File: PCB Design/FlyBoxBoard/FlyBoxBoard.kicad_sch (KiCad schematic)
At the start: 42 parts, among them J1 5V in, J10 RED, J11 GREEN, J12 WHITE, J13 INFRARED, J14 LCD Screen, J15 SD card reader, J16 5K Ohms, J17 5K Ohms, J18 ESP 32 Left Side extra pinouts, J19 ESP 32 Left Side extra pinouts, J2 12V in, J20 Transistor, J21 Logic Level LV pins, J22 Potentiometer, J23 Logic Level Left Side LV, J25 ESP 32 Right Side extra pinou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, J26 BuckPuck IR, J27 Logic Level Right Side HV, J28 Logic Level HV pins, J29 5K Ohms, J3 ESP 32 Left Side, J30 5K Ohms, J31 5K Ohms, J32 5K Ohms, J33 5K Ohms, J34 5K Ohms, J35 Transistor, J36 Transistor, J37 Transistor, J38 BuckPuck White, J39 BuckPuck Green, J4 Real Time Controller, J40 BuckPuck Red, J5 ESP 32 Right Side, J6 Rotary Knob, J9 FANS

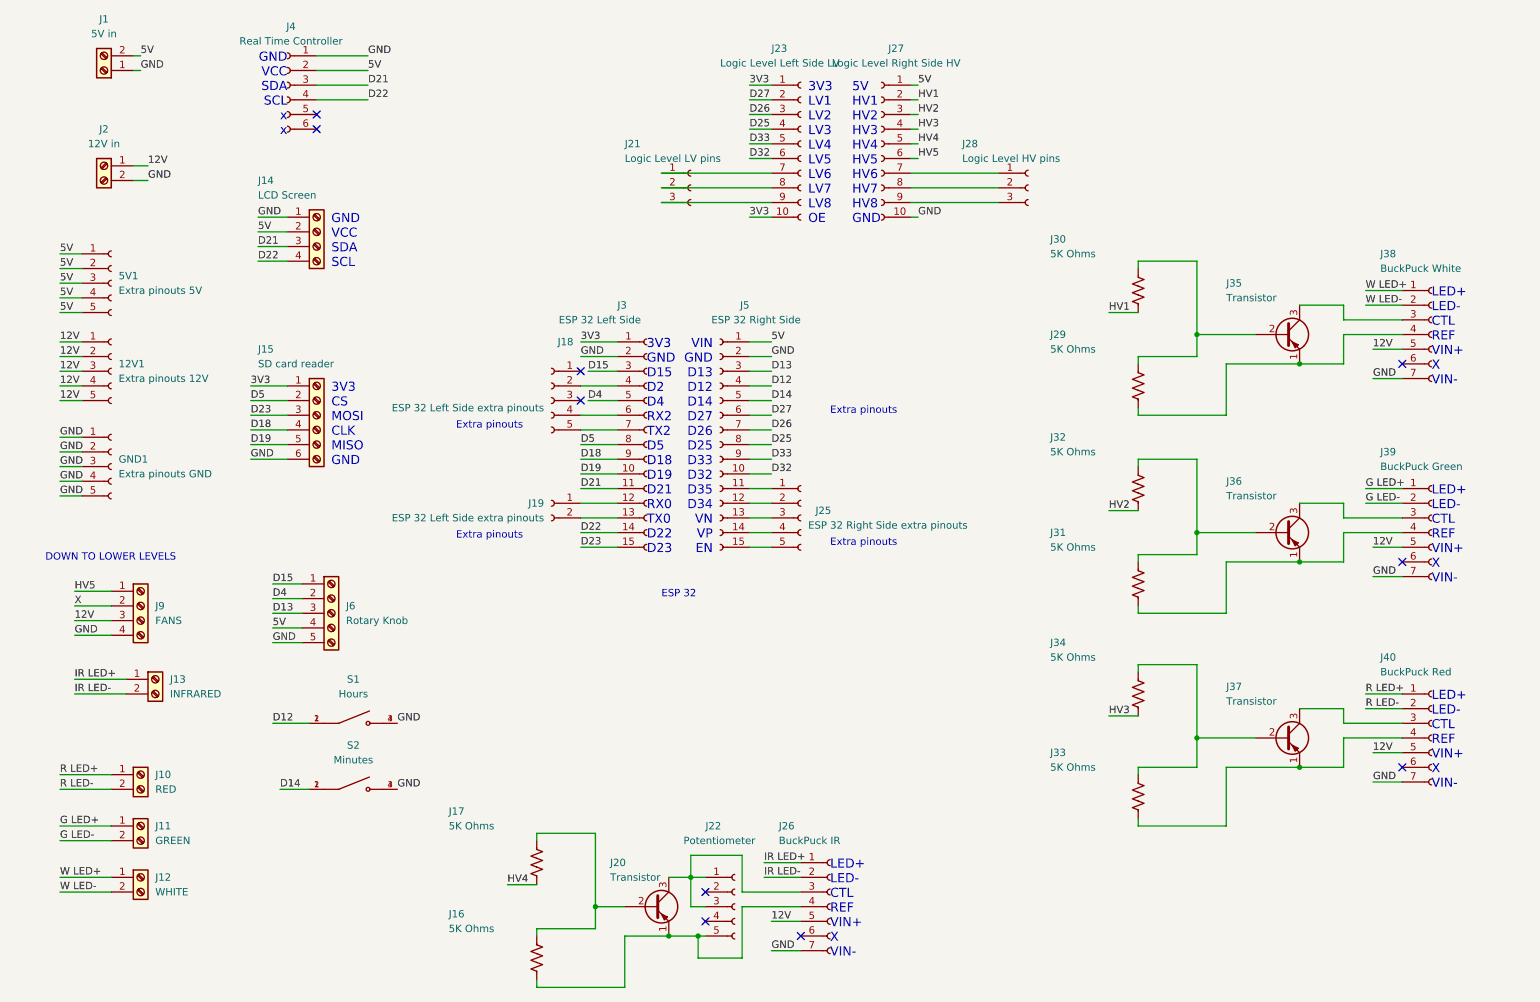
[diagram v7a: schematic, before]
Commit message: Shrunk vias, fixed ohms and XV1 labels
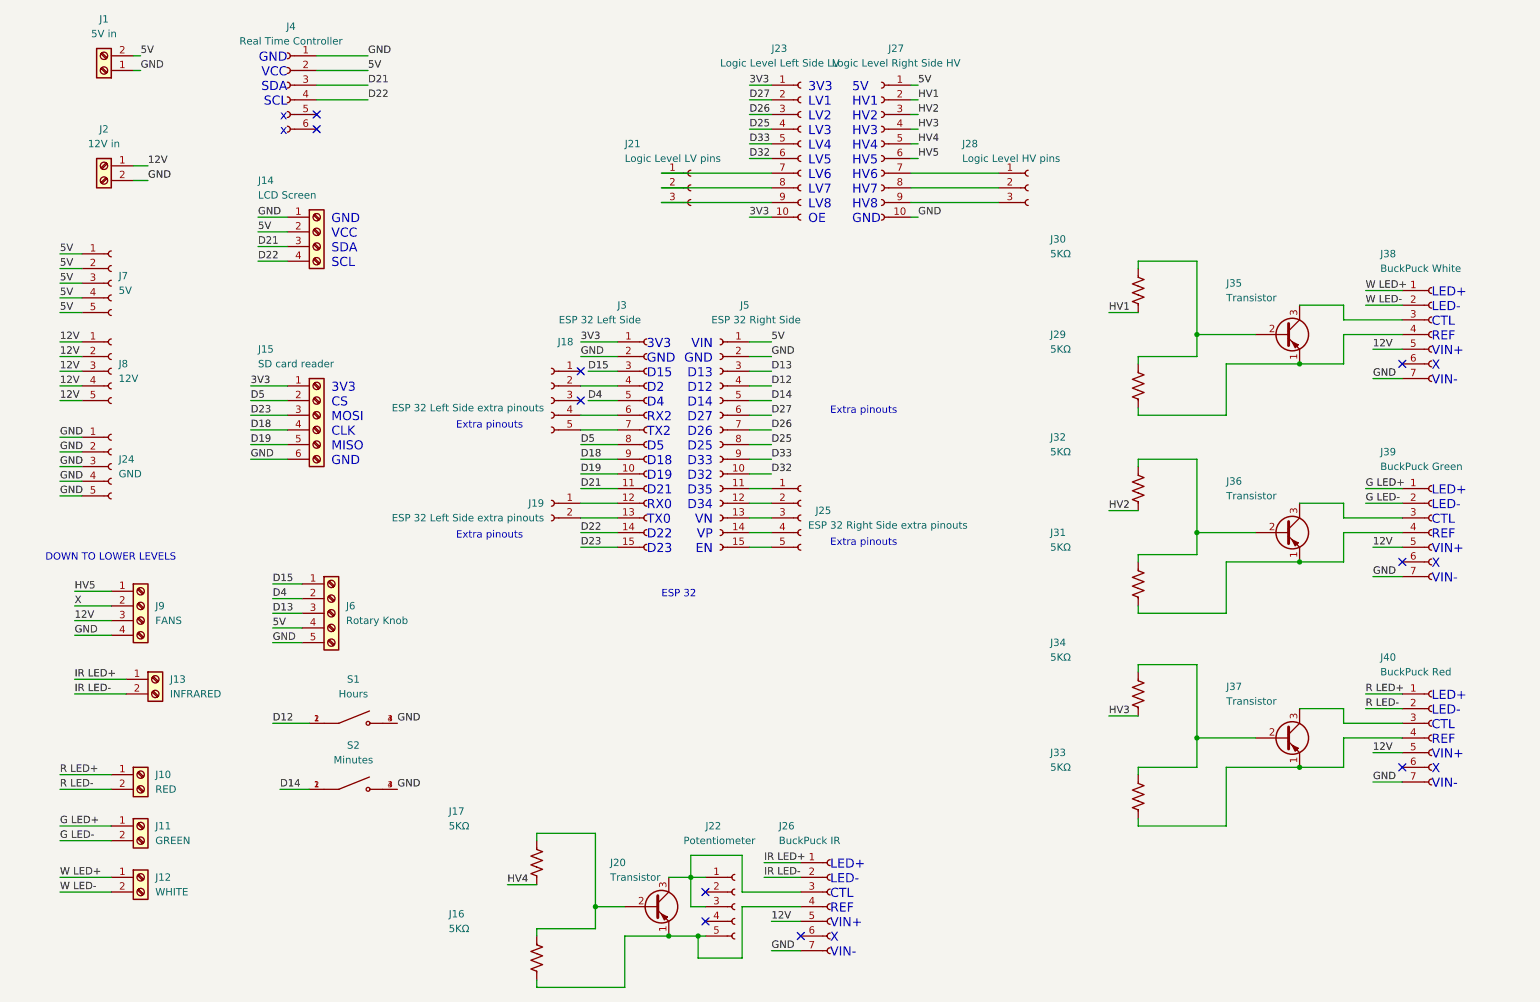
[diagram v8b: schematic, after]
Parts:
- J16, J17, J29, J30, J31, J32, J33, J34: value 5K Ohms -> 5KΩ
- J24: renamed from GND1; value Extra pinouts GND -> GND
- J7: renamed from 5V1; value Extra pinouts 5V -> 5V
- J8: renamed from 12V1; value Extra pinouts 12V -> 12V
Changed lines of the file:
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@@
   (symbol (lib_id "Connector:Conn_01x05_Female") (at 26.67 64.77 0) (unit 1)
     (in_bom yes) (on_board yes) (fields_autoplaced)
-    (property "Reference" "5V1" (id 0) (at 27.94 63.4999 0)
-      (effects (font (size 1.27 1.27)) (justify left))
-    )
-    (property "Value" "Extra pinouts 5V" (id 1) (at 27.94 66.0399 0)
+    (property "Reference" "J7" (id 0) (at 27.94 63.4999 0)
+      (effects (font (size 1.27 1.27)) (justify left))
+    )
+    (property "Value" "5V" (id 1) (at 27.94 66.0399 0)
       (effects (font (size 1.27 1.27)) (justify left))
     )
@@
       (effects (font (size 1.27 1.27)) (justify left))
     )
-    (property "Value" "5K Ohms" (id 1) (at 189.23 110.49 0)
+    (property "Value" "5KΩ" (id 1) (at 189.23 110.49 0)
       (effects (font (size 1.27 1.27)) (justify left))
     )
@@
       (effects (font (size 1.27 1.27)) (justify left))
     )
-    (property "Value" "5K Ohms" (id 1) (at 189.23 76.2 0)
+    (property "Value" "5KΩ" (id 1) (at 189.23 76.2 0)
       (effects (font (size 1.27 1.27)) (justify left))
     )
@@
   (symbol (lib_id "Connector:Conn_01x05_Female") (at 26.67 80.01 0) (unit 1)
     (in_bom yes) (on_board yes) (fields_autoplaced)
-    (property "Reference" "12V1" (id 0) (at 27.94 78.7399 0)
-      (effects (font (size 1.27 1.27)) (justify left))
-    )
-    (property "Value" "Extra pinouts 12V" (id 1) (at 27.94 81.2799 0)
+    (property "Reference" "J8" (id 0) (at 27.94 78.7399 0)
+      (effects (font (size 1.27 1.27)) (justify left))
+    )
+    (property "Value" "12V" (id 1) (at 27.94 81.2799 0)
       (effects (font (size 1.27 1.27)) (justify left))
     )
@@
   (symbol (lib_id "Connector:Conn_01x05_Female") (at 26.67 96.52 0) (unit 1)
     (in_bom yes) (on_board yes) (fields_autoplaced)
-    (property "Reference" "GND1" (id 0) (at 27.94 95.2499 0)
-      (effects (font (size 1.27 1.27)) (justify left))
-    )
-    (property "Value" "Extra pinouts GND" (id 1) (at 27.94 97.7899 0)
+    (property "Reference" "J24" (id 0) (at 27.94 95.2499 0)
+      (effects (font (size 1.27 1.27)) (justify left))
+    )
+    (property "Value" "GND" (id 1) (at 27.94 97.7899 0)
       (effects (font (size 1.27 1.27)) (justify left))
     )
@@
       (effects (font (size 1.27 1.27)) (justify left))
     )
-    (property "Value" "5K Ohms" (id 1) (at 189.23 148.59 0)
+    (property "Value" "5KΩ" (id 1) (at 189.23 148.59 0)
       (effects (font (size 1.27 1.27)) (justify left))
     )
@@
       (effects (font (size 1.27 1.27)) (justify left))
     )
-    (property "Value" "5K Ohms" (id 1) (at 189.23 59.69 0)
+    (property "Value" "5KΩ" (id 1) (at 189.23 59.69 0)
       (effects (font (size 1.27 1.27)) (justify left))
     )
@@
       (effects (font (size 1.27 1.27)) (justify left))
     )
-    (property "Value" "5K Ohms" (id 1) (at 85.09 176.53 0)
+    (property "Value" "5KΩ" (id 1) (at 85.09 176.53 0)
       (effects (font (size 1.27 1.27)) (justify left))
     )
@@
       (effects (font (size 1.27 1.27)) (justify left))
     )
-    (property "Value" "5K Ohms" (id 1) (at 189.23 129.54 0)
+    (property "Value" "5KΩ" (id 1) (at 189.23 129.54 0)
       (effects (font (size 1.27 1.27)) (justify left))
     )
@@
       (effects (font (size 1.27 1.27)) (justify left))
     )
-    (property "Value" "5K Ohms" (id 1) (at 189.23 93.98 0)
+    (property "Value" "5KΩ" (id 1) (at 189.23 93.98 0)
       (effects (font (size 1.27 1.27)) (justify left))
     )
@@
       (effects (font (size 1.27 1.27)) (justify left))
     )
-    (property "Value" "5K Ohms" (id 1) (at 85.09 158.75 0)
+    (property "Value" "5KΩ" (id 1) (at 85.09 158.75 0)
       (effects (font (size 1.27 1.27)) (justify left))
     )
@@
   )
   (symbol_instances
-    (path "/2481291e-206f-4136-b767-c88851d692f7"
-      (reference "5V1") (unit 1) (value "Extra pinouts 5V") (footprint "Connector_PinSocket_2.54mm:PinSocket_1x05_P2.54mm_Vertical")
-    )
-    (path "/6183f4c2-b8b4-40db-bb6c-bf761daf770e"
-      (reference "12V1") (unit 1) (value "Extra pinouts 12V") (footprint "Connector_PinSocket_2.54mm:PinSocket_1x05_P2.54mm_Vertical")
-    )
-    (path "/89950f7f-7114-4cb1-ae2e-fc47480a7284"
-      (reference "GND1") (unit 1) (value "Extra pinouts GND") (footprint "Connector_PinSocket_2.54mm:PinSocket_1x05_P2.54mm_Vertical")
-    )
     (path "/44c71451-ea99-4268-833f-b68e3d908475"
       (reference "J1") (unit 1) (value "5V in") (footprint "TerminalBlock:TerminalBlock_bornier-2_P5.08mm")
@@
       (reference "J6") (unit 1) (value "Rotary Knob") (footprint "TerminalBlock:TerminalBlock_bornier-5_P5.08mm")
     )
+    (path "/2481291e-206f-4136-b767-c88851d692f7"
+      (reference "J7") (unit 1) (value "5V") (footprint "Connector_PinSocket_2.54mm:PinSocket_1x05_P2.54mm_Vertical")
+    )
+    (path "/6183f4c2-b8b4-40db-bb6c-bf761daf770e"
+      (reference "J8") (unit 1) (value "12V") (footprint "Connector_PinSocket_2.54mm:PinSocket_1x05_P2.54mm_Vertical")
+    )
     (path "/bbae7729-1b1d-4e0d-b021-77b9c2200ef4"
       (reference "J9") (unit 1) (value "FANS") (footprint "TerminalBlock:TerminalBlock_bornier-4_P5.08mm")
@@
     )
     (path "/c0473f3f-82e6-418a-b889-dfcb5651b6e1"
-      (reference "J16") (unit 1) (value "5K Ohms") (footprint "Resistor_SMD:R_0805_2012Metric_Pad1.20x1.40mm_HandSolder")
+      (reference "J16") (unit 1) (value "5KΩ") (footprint "Resistor_SMD:R_0805_2012Metric_Pad1.20x1.40mm_HandSolder")
     )
     (path "/d2ffe9e0-42cd-49d3-9622-5c200a1d4d6b"
-      (reference "J17") (unit 1) (value "5K Ohms") (footprint "Resistor_SMD:R_0805_2012Metric_Pad1.20x1.40mm_HandSolder")
+      (reference "J17") (unit 1) (value "5KΩ") (footprint "Resistor_SMD:R_0805_2012Metric_Pad1.20x1.40mm_HandSolder")
     )
     (path "/857e8bbb-d58b-44f9-ba40-ff0fb25a9518"
@@
       (reference "J23") (unit 1) (value "Logic Level Left Side LV") (footprint "Connector_PinSocket_2.54mm:PinSocket_1x10_P2.54mm_Vertical")
     )
+    (path "/89950f7f-7114-4cb1-ae2e-fc47480a7284"
+      (reference "J24") (unit 1) (value "GND") (footprint "Connector_PinSocket_2.54mm:PinSocket_1x05_P2.54mm_Vertical")
+    )
     (path "/108235f0-b9d5-497f-8a9f-f494ab16621f"
       (reference "J25") (unit 1) (value "ESP 32 Right Side extra pinouts") (footprint "Connector_PinSocket_2.54mm:PinSocket_1x05_P2.54mm_Vertical")
@@
     )
     (path "/60499b43-5f6c-4a6f-a2eb-3aa9716cc0ba"
-      (reference "J29") (unit 1) (value "5K Ohms") (footprint "Resistor_SMD:R_0805_2012Metric_Pad1.20x1.40mm_HandSolder")
+      (reference "J29") (unit 1) (value "5KΩ") (footprint "Resistor_SMD:R_0805_2012Metric_Pad1.20x1.40mm_HandSolder")
     )
     (path "/ab51f81b-b48f-4409-957f-b67378bdcc26"
-      (reference "J30") (unit 1) (value "5K Ohms") (footprint "Resistor_SMD:R_0805_2012Metric_Pad1.20x1.40mm_HandSolder")
+      (reference "J30") (unit 1) (value "5KΩ") (footprint "Resistor_SMD:R_0805_2012Metric_Pad1.20x1.40mm_HandSolder")
     )
     (path "/3bd62000-5fc9-4e92-b81f-1291db779a1c"
-      (reference "J31") (unit 1) (value "5K Ohms") (footprint "Resistor_SMD:R_0805_2012Metric_Pad1.20x1.40mm_HandSolder")
+      (reference "J31") (unit 1) (value "5KΩ") (footprint "Resistor_SMD:R_0805_2012Metric_Pad1.20x1.40mm_HandSolder")
     )
     (path "/d1e91425-de58-4d3b-8e51-3c6627014719"
-      (reference "J32") (unit 1) (value "5K Ohms") (footprint "Resistor_SMD:R_0805_2012Metric_Pad1.20x1.40mm_HandSolder")
+      (reference "J32") (unit 1) (value "5KΩ") (footprint "Resistor_SMD:R_0805_2012Metric_Pad1.20x1.40mm_HandSolder")
     )
     (path "/a94e9539-ec64-4626-90c7-2d5b23824f3d"
-      (reference "J33") (unit 1) (value "5K Ohms") (footprint "Resistor_SMD:R_0805_2012Metric_Pad1.20x1.40mm_HandSolder")
+      (reference "J33") (unit 1) (value "5KΩ") (footprint "Resistor_SMD:R_0805_2012Metric_Pad1.20x1.40mm_HandSolder")
     )
     (path "/c0f2639e-9c85-4418-a96f-12a5ede5b682"
-      (reference "J34") (unit 1) (value "5K Ohms") (footprint "Resistor_SMD:R_0805_2012Metric_Pad1.20x1.40mm_HandSolder")
+      (reference "J34") (unit 1) (value "5KΩ") (footprint "Resistor_SMD:R_0805_2012Metric_Pad1.20x1.40mm_HandSolder")
     )
     (path "/339a0dfd-7e42-4fb8-aac5-3fbb443de980"
